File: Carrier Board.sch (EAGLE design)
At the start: 53 parts, among them J4 S2B-PH-SM4-TB(LF)(SN), J5 S2B-PH-SM4-TB(LF)(SN), Q1 MMBT2222A, SW2 MF-SW-TACT-6MM, U1 TMP36GRTZ, U2 TPL5010, U3 MB85RC256, U7 NAND

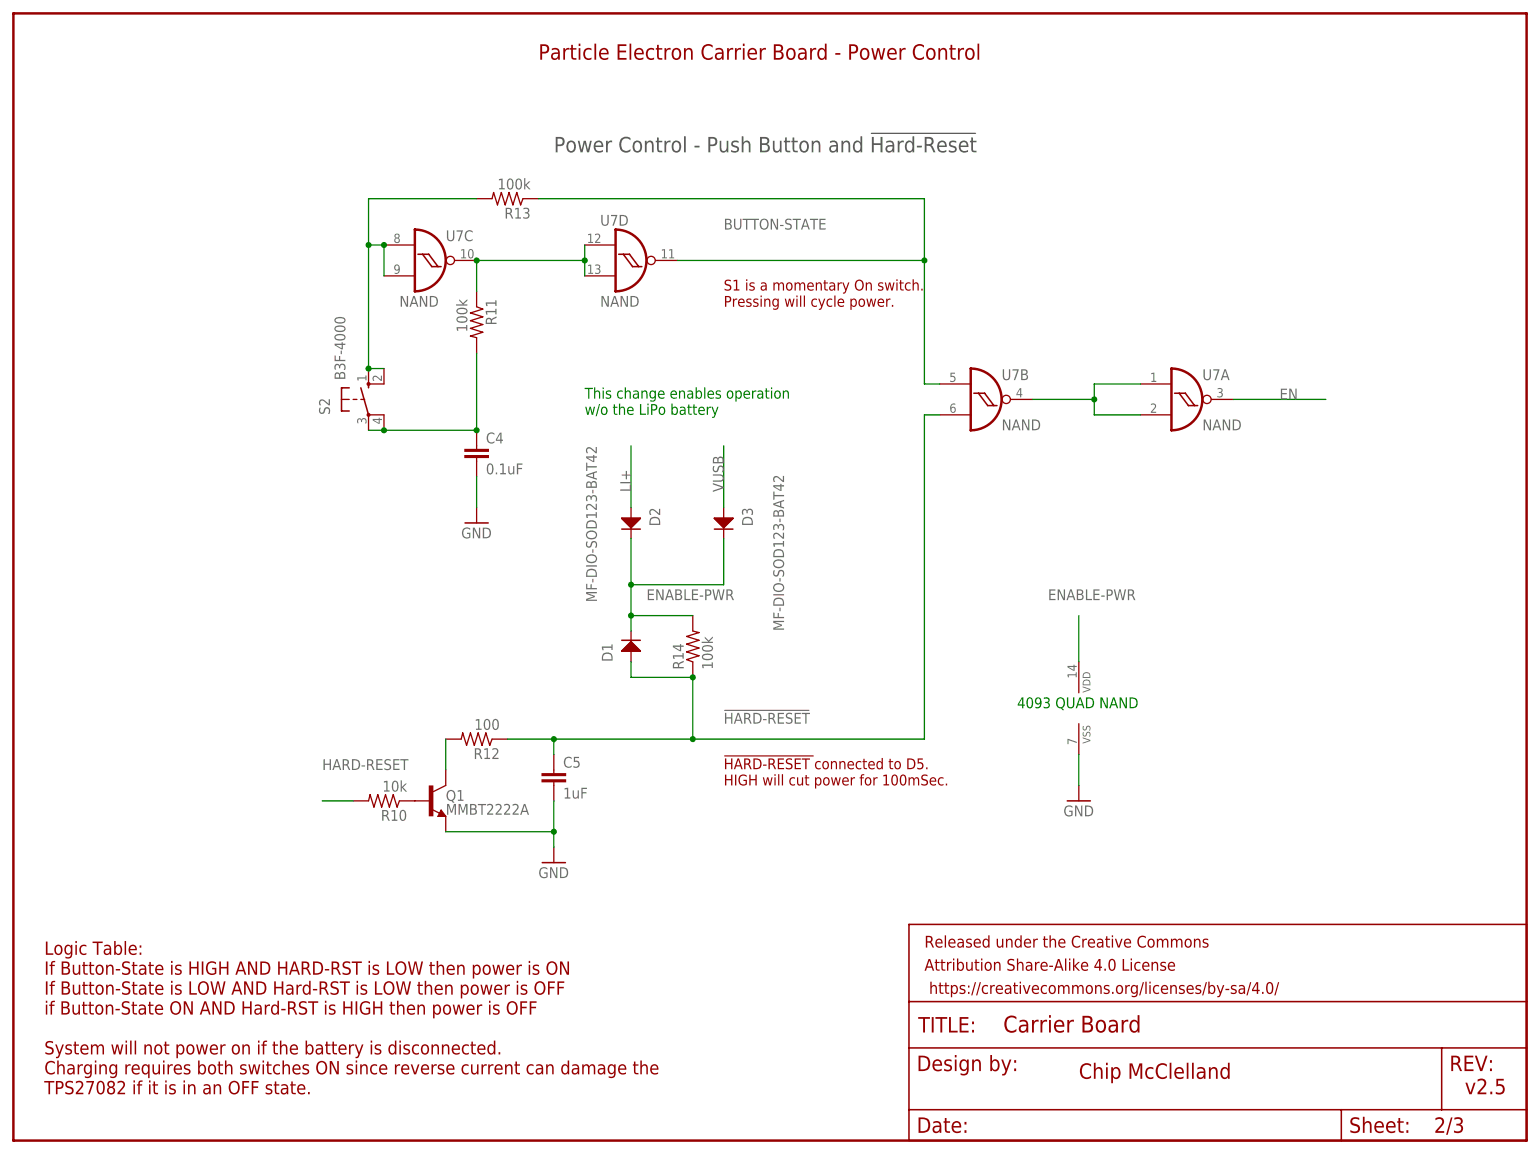
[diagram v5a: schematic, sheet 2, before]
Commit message: Labelling and less traces under the chips
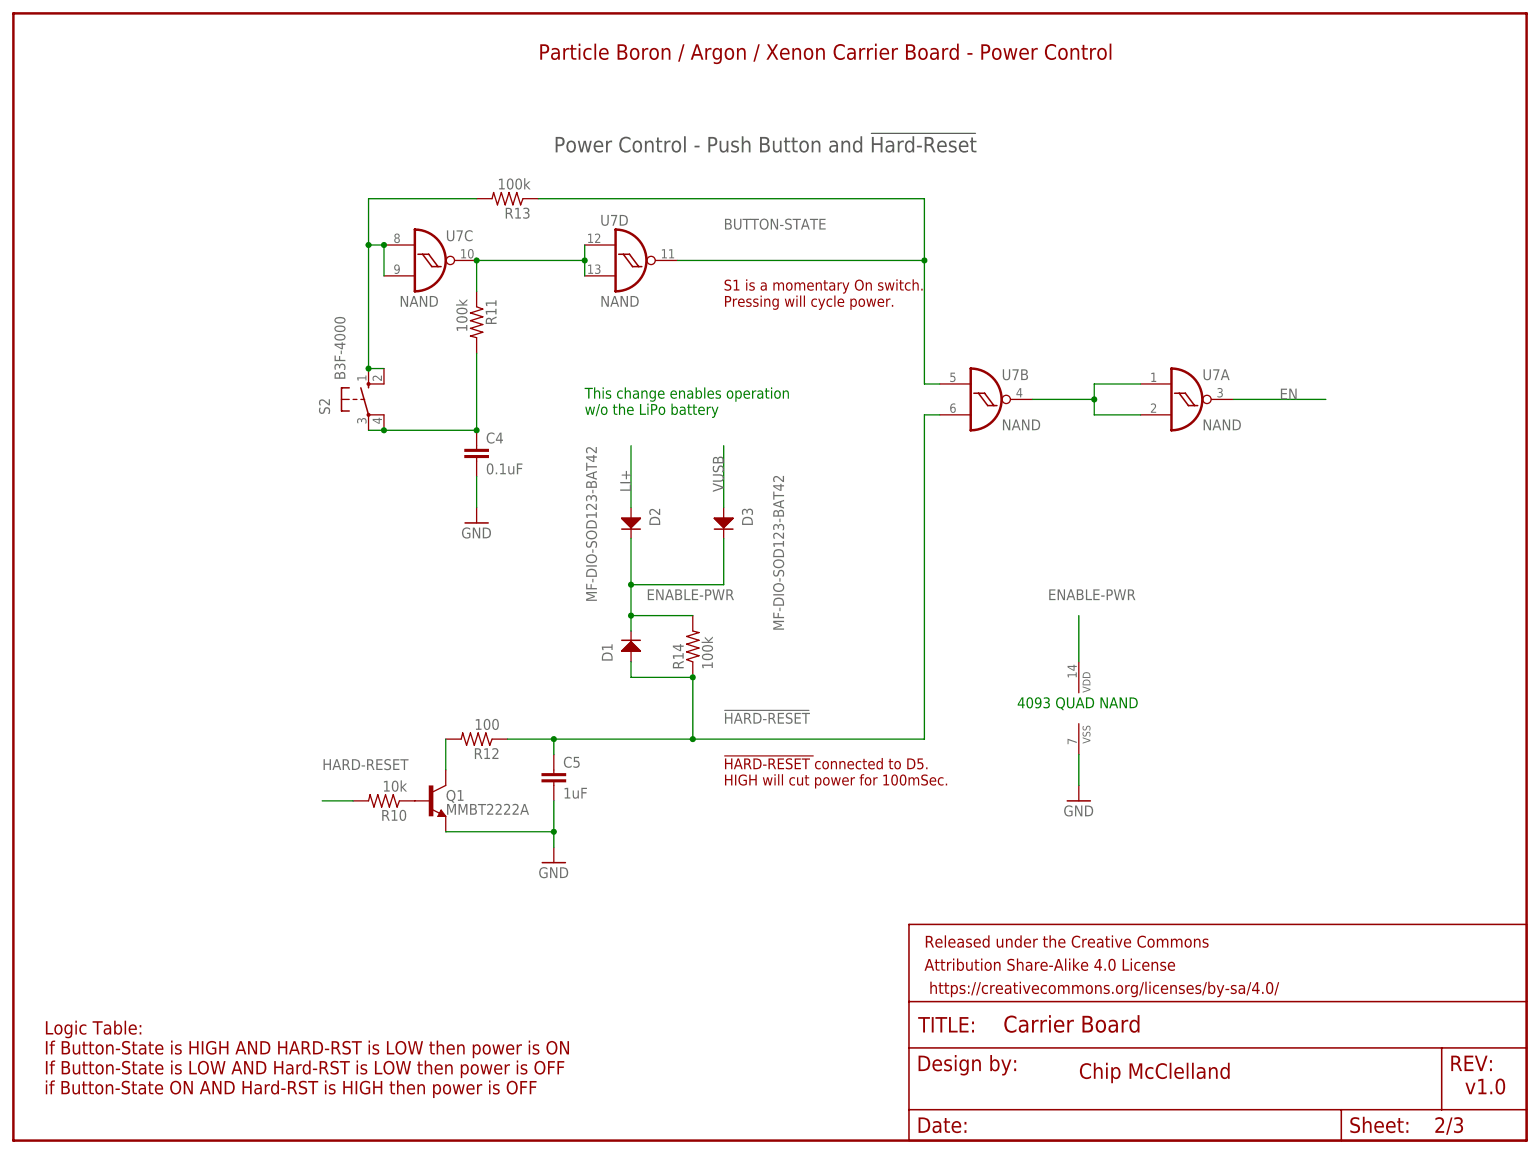
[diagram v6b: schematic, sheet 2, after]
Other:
- note added: "Device TPS62291 has short circuit protection. Vin is protected by F1"
- note added: "Logic Table: If Button-State is HIGH AND HARD-RST is LOW then power is ON If Button-State is LOW AND Hard-RST is LOW then power is OFF if Button-State ON AND Hard-RST is HIGH then power is OFF"
- note added: "Particle Boron / Argon / Xenon Carrier Board - Power Control"
- note added: "Particle Boron / Xenon / Argon Carrier Board - Power Protection"
- note added: "Particle Boron / Xenon / Argon Carrier Board for Unprotected Environments"
- note added: "v1.0"
- note removed: "Electron's TPS62291 has short circuit protection. Vin is protected by F1"
- note removed: "Logic Table: If Button-State is HIGH AND HARD-RST is LOW then power is ON If Button-State is LOW AND Hard-RST is LOW then power is OFF if Button-State ON AND Hard-RST is HIGH then power is OFF System will not power on if the battery is disconnected. Charging requires both switches ON since reverse current can damage the TPS27082 if it is in an OFF state."
- note removed: "Particle Electron Carrier Board - Power Control"
- note removed: "Particle Electron Carrier Board - Power Protection"
- note removed: "Particle Electron Carrier Board for Unprotected Environments"
- note removed: "v2.5"
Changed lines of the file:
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@@
 <text x="172.72" y="7.62" size="1.778" layer="94">Chip McClelland
 chip@mcclellands.org</text>
-<text x="238.76" y="7.62" size="2.54" layer="94">v2.5</text>
+<text x="238.76" y="7.62" size="2.54" layer="94">v1.0</text>
 <text x="149.86" y="38.1" size="1.778" layer="94">Power either with DC source or Solar Panel - JST connector
 1) External Power: 5V DC @ 2A
 2) Solar Power: Recommend 3-5W @ 6V</text>
-<text x="63.5" y="180.34" size="2.54" layer="94" ratio="10">Particle Electron Carrier Board for Unprotected Environments</text>
+<text x="63.5" y="180.34" size="2.54" layer="94" ratio="10">Particle Boron / Xenon / Argon Carrier Board for Unprotected Environments</text>
 <text x="12.7" y="60.96" size="1.778" layer="94">R1 and R2 values set reset interval.
 See pages 12-13 in manual for values
@@
 <description>Power Control</description>
 <plain>
-<text x="86.36" y="177.8" size="2.54" layer="94" ratio="10">Particle Electron Carrier Board - Power Control</text>
+<text x="86.36" y="177.8" size="2.54" layer="94" ratio="10">Particle Boron / Argon / Xenon Carrier Board - Power Control</text>
 <text x="165.1" y="71.12" size="1.778" layer="91">4093 QUAD NAND</text>
 <text x="88.9" y="162.56" size="2.54" layer="97">Power Control - Push Button and !Hard-Reset</text>
 <text x="175.26" y="10.16" size="2.54" layer="94">Chip McClelland</text>
-<text x="238.76" y="7.62" size="2.54" layer="94">v2.5</text>
+<text x="238.76" y="7.62" size="2.54" layer="94">v1.0</text>
 <text x="5.08" y="7.62" size="2.1844" layer="94">Logic Table:
 If Button-State is HIGH AND HARD-RST is LOW then power is ON
 If Button-State is LOW AND Hard-RST is LOW then power is OFF
 if Button-State ON AND Hard-RST is HIGH then power is OFF
-System will not power on if the battery is disconnected.
-Charging requires both switches ON since reverse current can damage the
-TPS27082 if it is in an OFF state.
 </text>
 <text x="116.84" y="58.42" size="1.778" layer="94">!HARD-RESET !connected to D5.
@@
 <plain>
 <text x="129.54" y="68.58" size="2.54" layer="97" rot="R90">Protection Circuits for External Connections</text>
-<text x="68.58" y="127" size="2.54" layer="97">Electron's TPS62291 has
+<text x="68.58" y="127" size="2.54" layer="97">Device TPS62291 has
 short circuit protection.
 Vin is protected by F1</text>
 <text x="175.26" y="10.16" size="2.54" layer="94">Chip McClelland</text>
-<text x="238.76" y="7.62" size="2.54" layer="94">v2.5</text>
-<text x="83.82" y="177.8" size="2.54" layer="94">Particle Electron Carrier Board - Power Protection</text>
+<text x="238.76" y="7.62" size="2.54" layer="94">v1.0</text>
+<text x="83.82" y="177.8" size="2.54" layer="94">Particle Boron / Xenon / Argon Carrier Board - Power Protection</text>
 </plain>
 <instances>

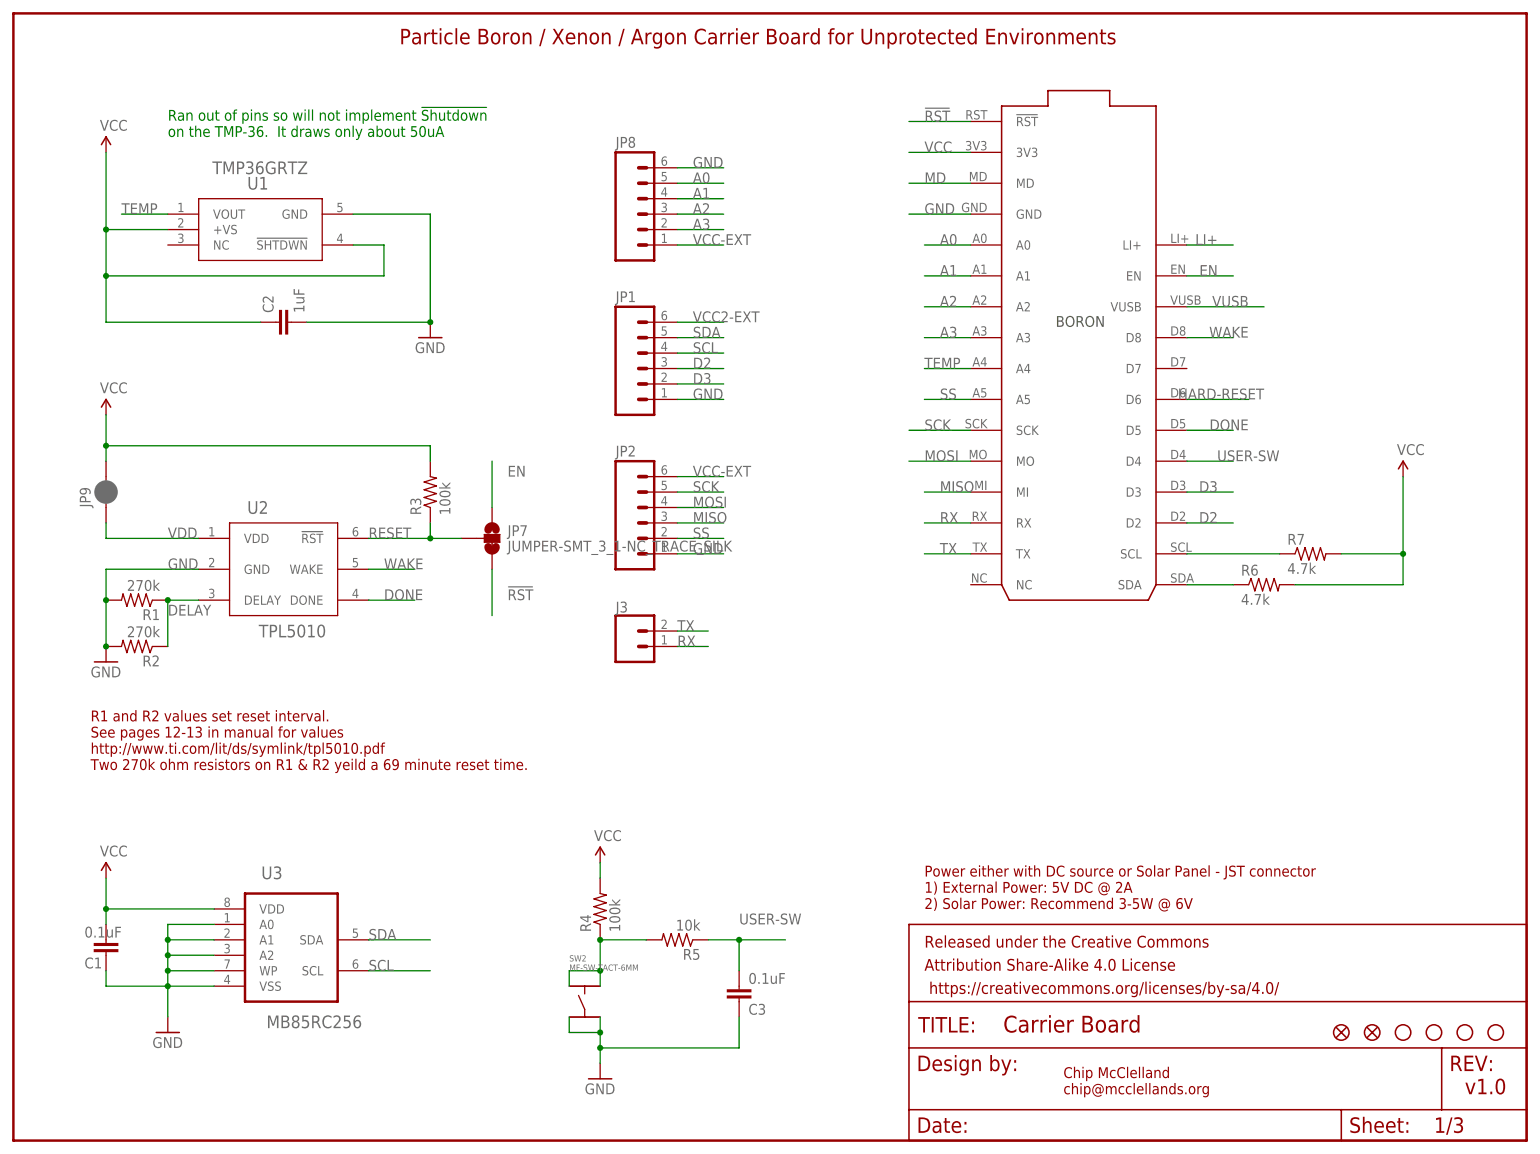
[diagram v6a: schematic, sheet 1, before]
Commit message: Added 2-Grove Connectors
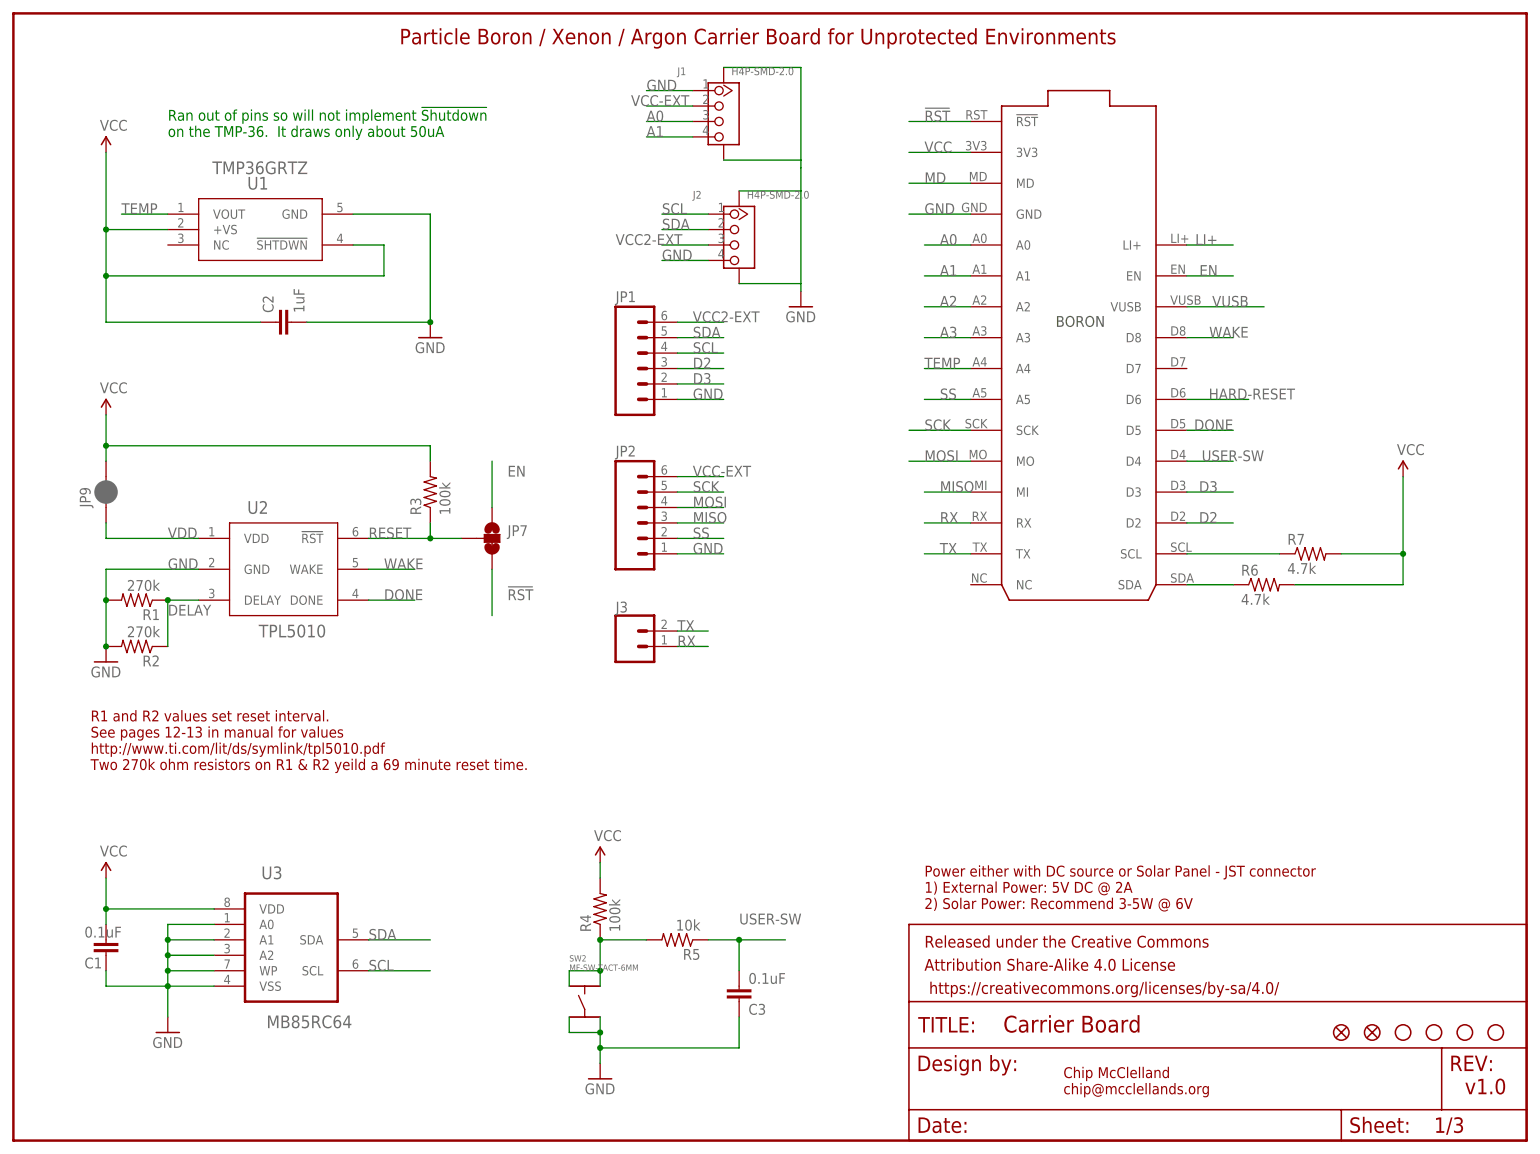
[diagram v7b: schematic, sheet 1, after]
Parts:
- removed JP8: (no value), SparkFun-Connectors:M06LOCK
- added J1, J2: H4P-SMD-2.0, OPL_Connector:GROVE-CONNECTOR-SMD(4+2P-2.0)
- U3: value MB85RC256 -> MB85RC64
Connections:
- net A0: now also J1.3; no longer JP8.5
- net A1: now also J1.4; no longer JP8.4
- net A2: no longer JP8.3
- net A3: no longer JP8.2
- net GND: now also J1.1, J1.SS1, J1.SS2, J2.4, J2.SS1, J2.SS2; no longer JP8.6
- net SCL: now also J2.1
- net SDA: now also J2.2
- net VCC-EXT: now also J1.2; no longer JP8.1
- net VCC2-EXT: now also J2.3
